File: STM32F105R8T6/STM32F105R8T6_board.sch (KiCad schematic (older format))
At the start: 34 parts, among them J2 DC_POWER_JACK, SW1 SW_PUSH, U1 STM32F105R8T6, U2 1117, X1 CRYSTAL, X2 CRYSTAL

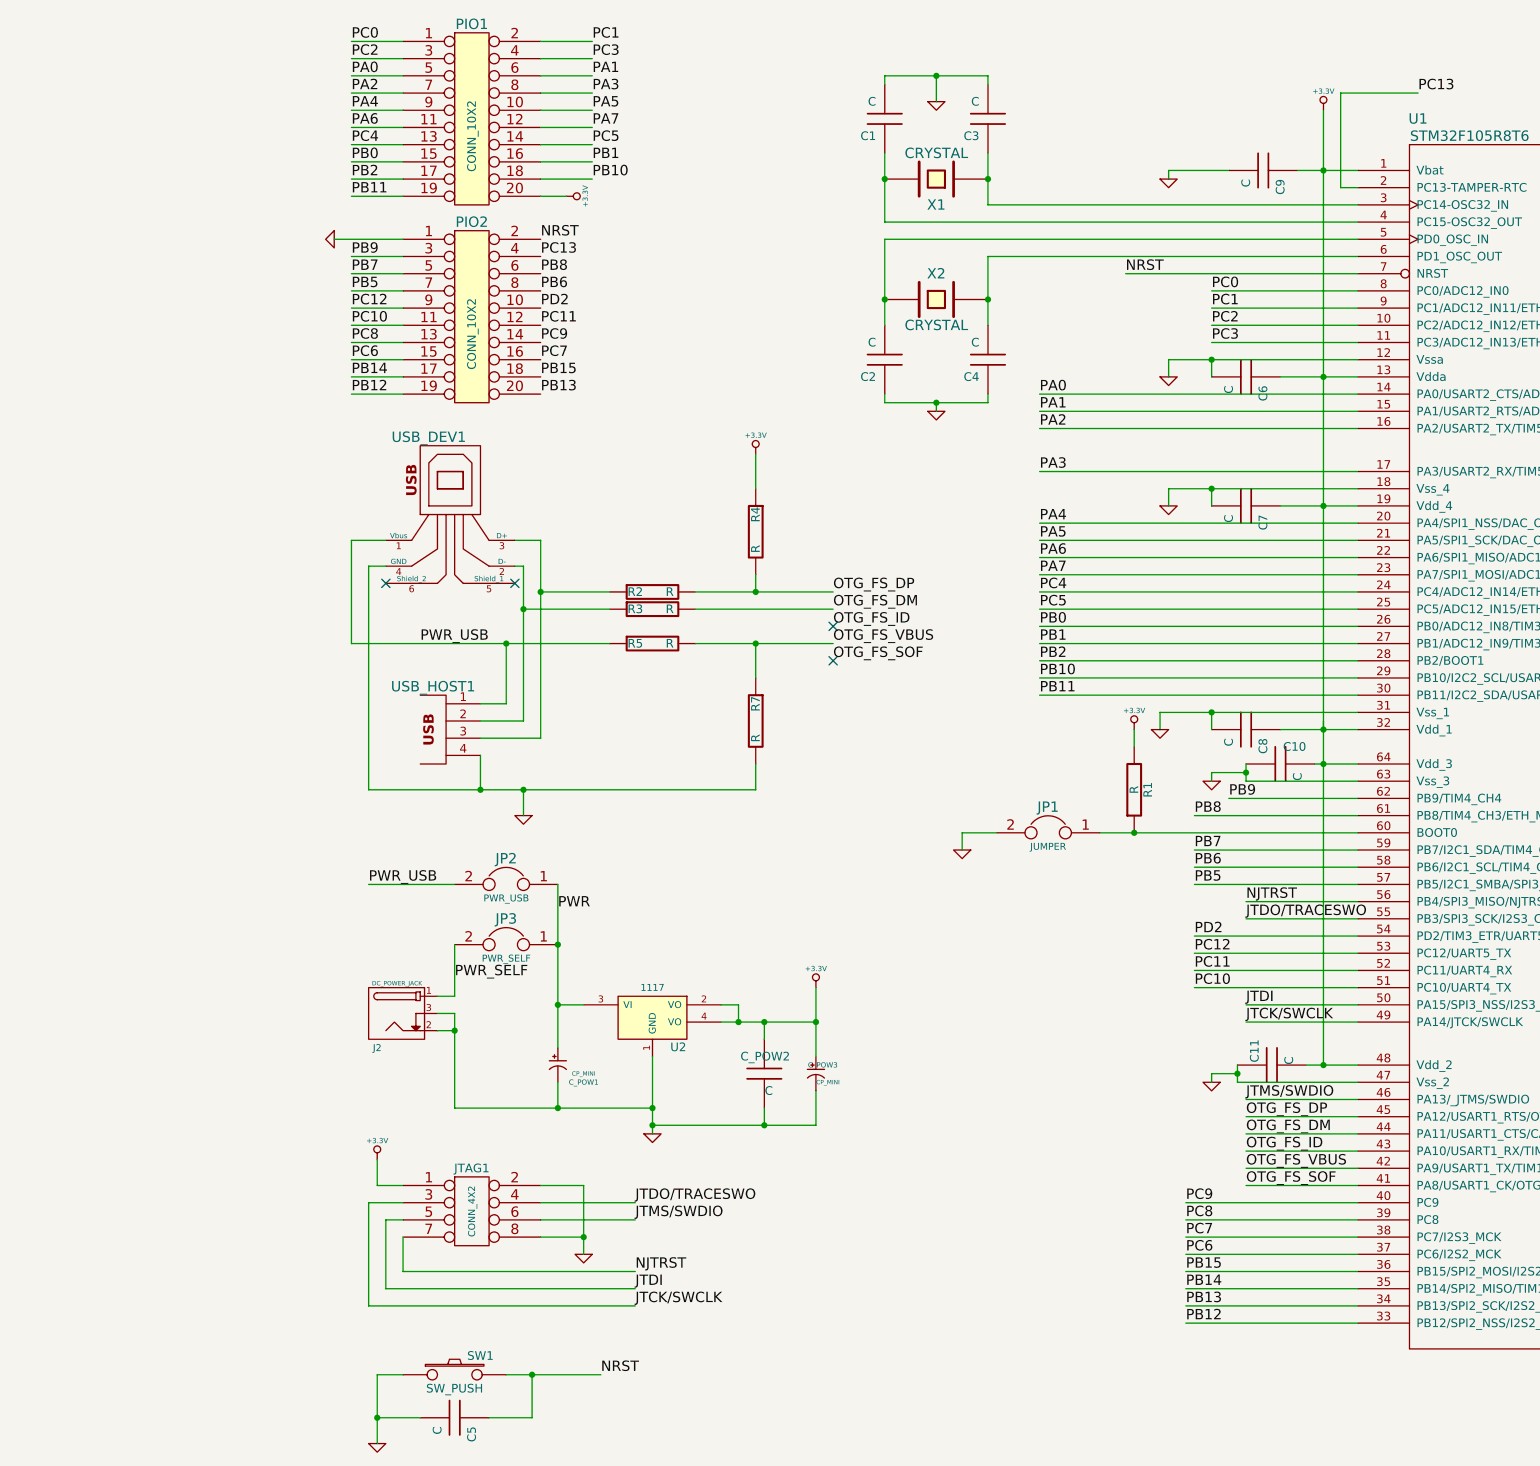
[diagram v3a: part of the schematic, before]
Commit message: Reruteo a 10mils/9.6mils en placas LPC1754 y STM32F105R8T6
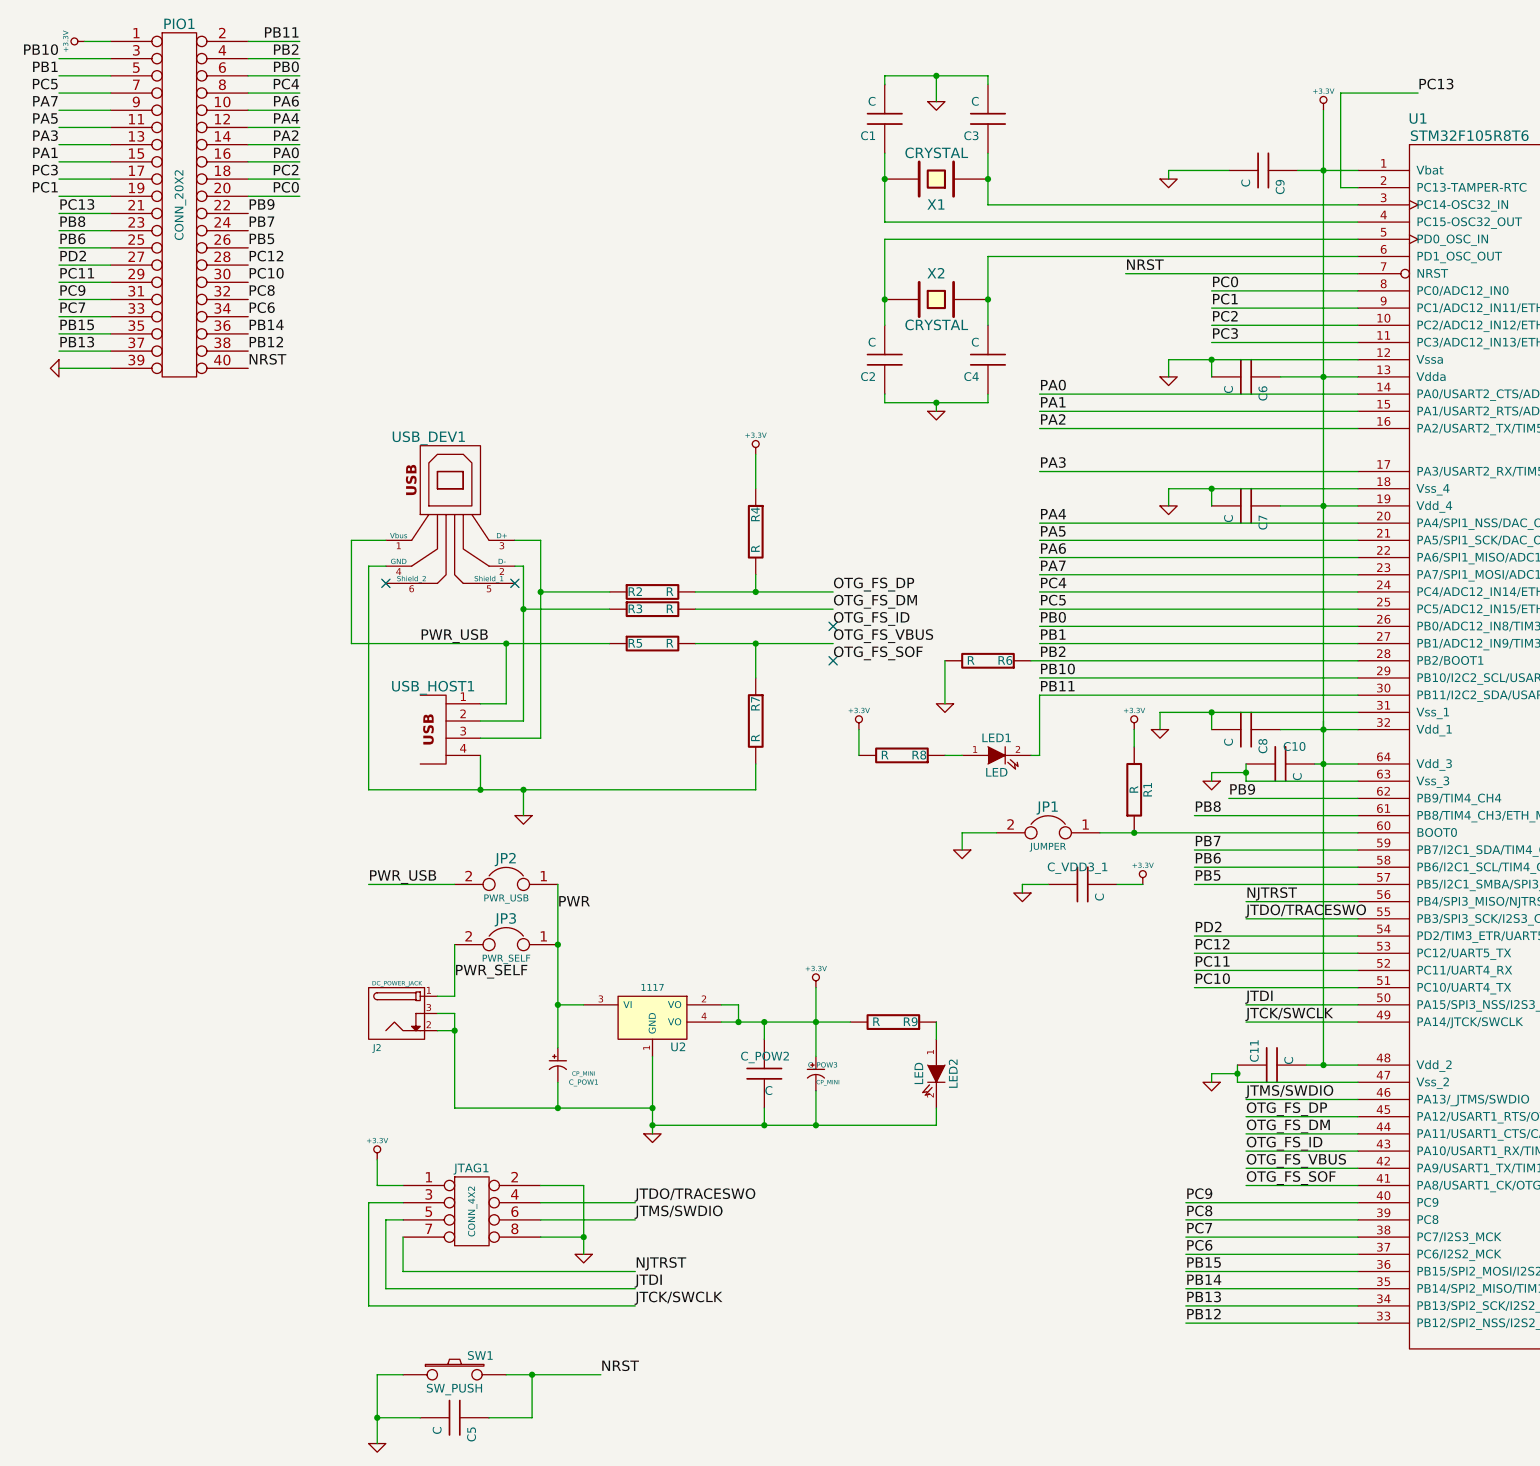
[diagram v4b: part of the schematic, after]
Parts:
- removed PIO1, PIO2: CONN_10X2, symbol CONN_10X2
- added C_VDD3_1: C, symbol C
- added LED1, LED2: LED, symbol LED
- added PIO1: CONN_20X2, symbol CONN_20X2
- added R6, R8, R9: R, symbol R
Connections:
- net +3.3V: now also C_VDD3_1.2, PIO1.1 (P1), R8.2, R9.2
- net GND: now also C_VDD3_1.1, LED2.2 (K), PIO1.39 (P39), R6.2
- net NRST: now also PIO1.40 (P40)
- net PA0: now also PIO1.16 (P16)
- net PA1: now also PIO1.15 (P15)
- net PA2: now also PIO1.14 (P14)
- net PA3: now also PIO1.13 (P13)
- net PA4: now also PIO1.12 (P12)
- net PA5: now also PIO1.11 (P11)
- net PA6: now also PIO1.10 (P10)
- net PA7: now also PIO1.9 (P9)
- net PB0: now also PIO1.6 (P6)
- net PB1: now also PIO1.5 (P5)
- net PB10: now also PIO1.3 (P3)
- net PB11: now also LED1.2 (K), PIO1.2 (P2)
- net PB12: now also PIO1.38 (P38)
- net PB13: now also PIO1.37 (P37)
- net PB14: now also PIO1.36 (P36)
- net PB15: now also PIO1.35 (P35)
- net PB2: now also PIO1.4 (P4), R6.1
- net PB5: now also PIO1.26 (P26)
- net PB6: now also PIO1.25
- net PB7: now also PIO1.24 (P24)
- net PB8: now also PIO1.23 (P23)
- net PB9: now also PIO1.22 (P22)
- net PC0: now also PIO1.20 (P20)
- net PC1: now also PIO1.19 (P19)
- net PC10: now also PIO1.30 (P30)
- net PC11: now also PIO1.29 (P29)
- net PC12: now also PIO1.28 (P28)
- net PC13: now also PIO1.21 (P21)
- net PC2: now also PIO1.18 (P18)
- net PC3: now also PIO1.17 (P17)
- net PC4: now also PIO1.8 (P8)
- net PC5: now also PIO1.7 (P7)
- net PC6: now also PIO1.34 (P34)
- net PC7: now also PIO1.33 (P33)
- net PC8: now also PIO1.32 (P32)
- net PC9: now also PIO1.31 (P31)
- net PD2: now also PIO1.27 (P27)
- new net: LED1.1 (A), R8.1
- new net: LED2.1 (A), R9.1
